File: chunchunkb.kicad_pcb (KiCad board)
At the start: 2 copper layers, 143.7 x 119.1 mm, 124 parts, among them J1 BATT, J2 OLED, SW1 SW_Push, SW10 SW_Push, SW11 SW_Push, SW12 SW_Push, SW13 SW_Push, SW14 SW_Push, SW15 SW_Push, SW16 SW_Push, SW17 SW_Push, SW18 SW_Push, SW19 SW_Push, SW2 SW_Push, SW20 SW_Push, SW21 SW_Push, SW22 SW_Push, SW23 SW_Push, SW24 SW_Push, SW25 SW_Push, SW26 SW_Push, SW27 SW_Push, SW28 SW_Push, SW29 SW_Push, SW3 SW_Push, SW30 SW_Push, SW31 EC11, SW32 SW_Push, SW33 SW_Push, SW34 SW_Push, SW35 SW_Push, SW36 SW_Push, SW4 SW_Push, SW5 SW_Push, SW6 SW_Push, SW7 SW_Push, SW8 SW_Push, SW9 SW_Push

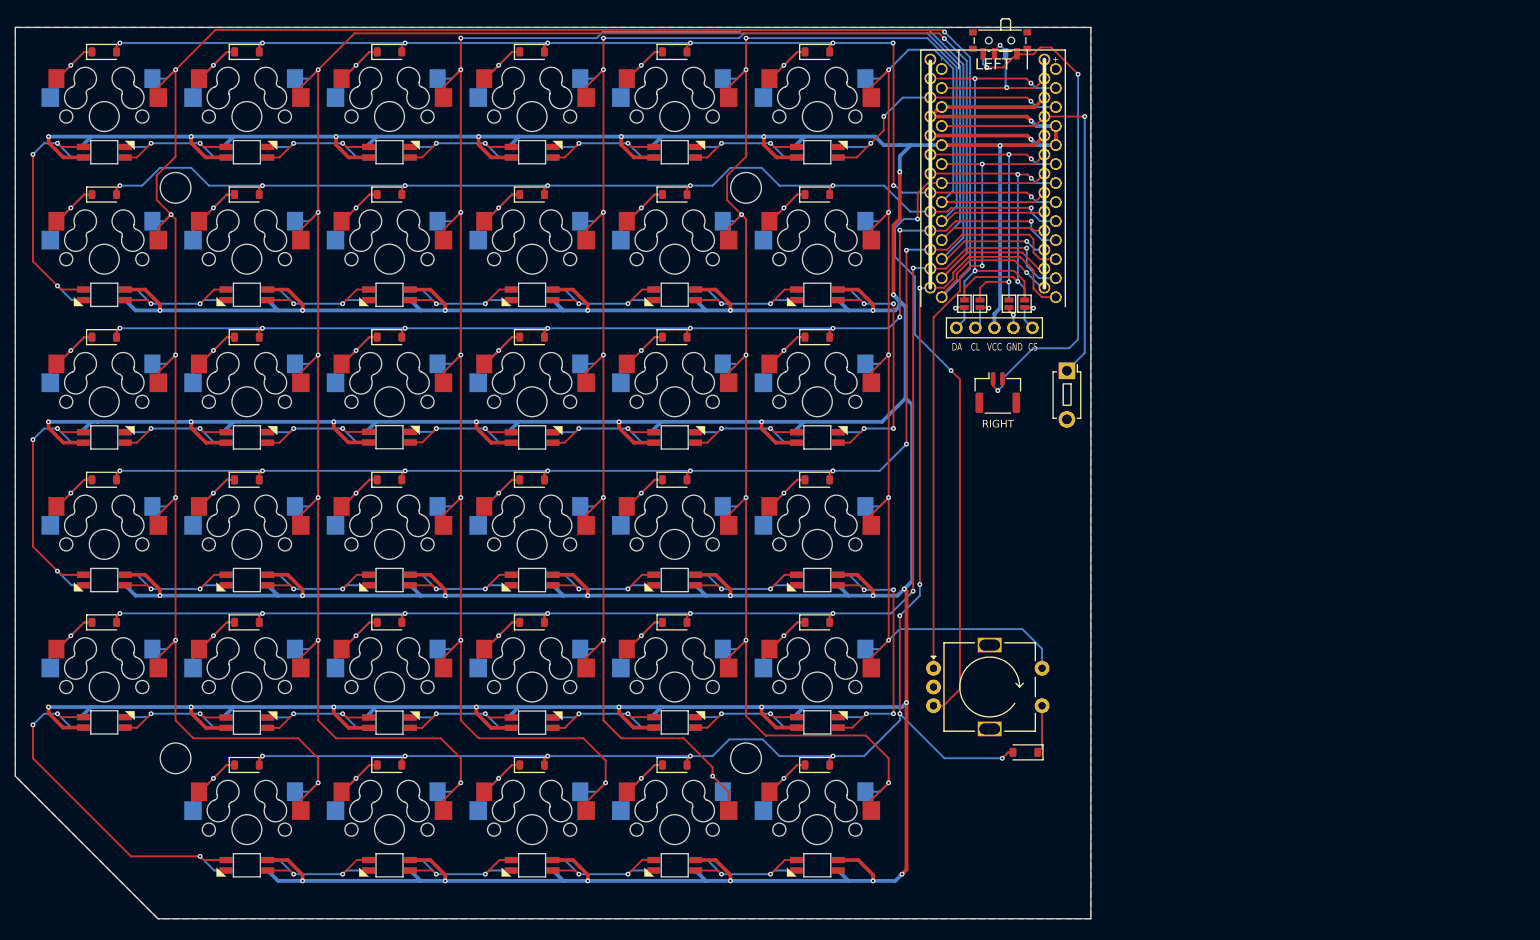
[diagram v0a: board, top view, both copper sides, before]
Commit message: feat: change space btn pos
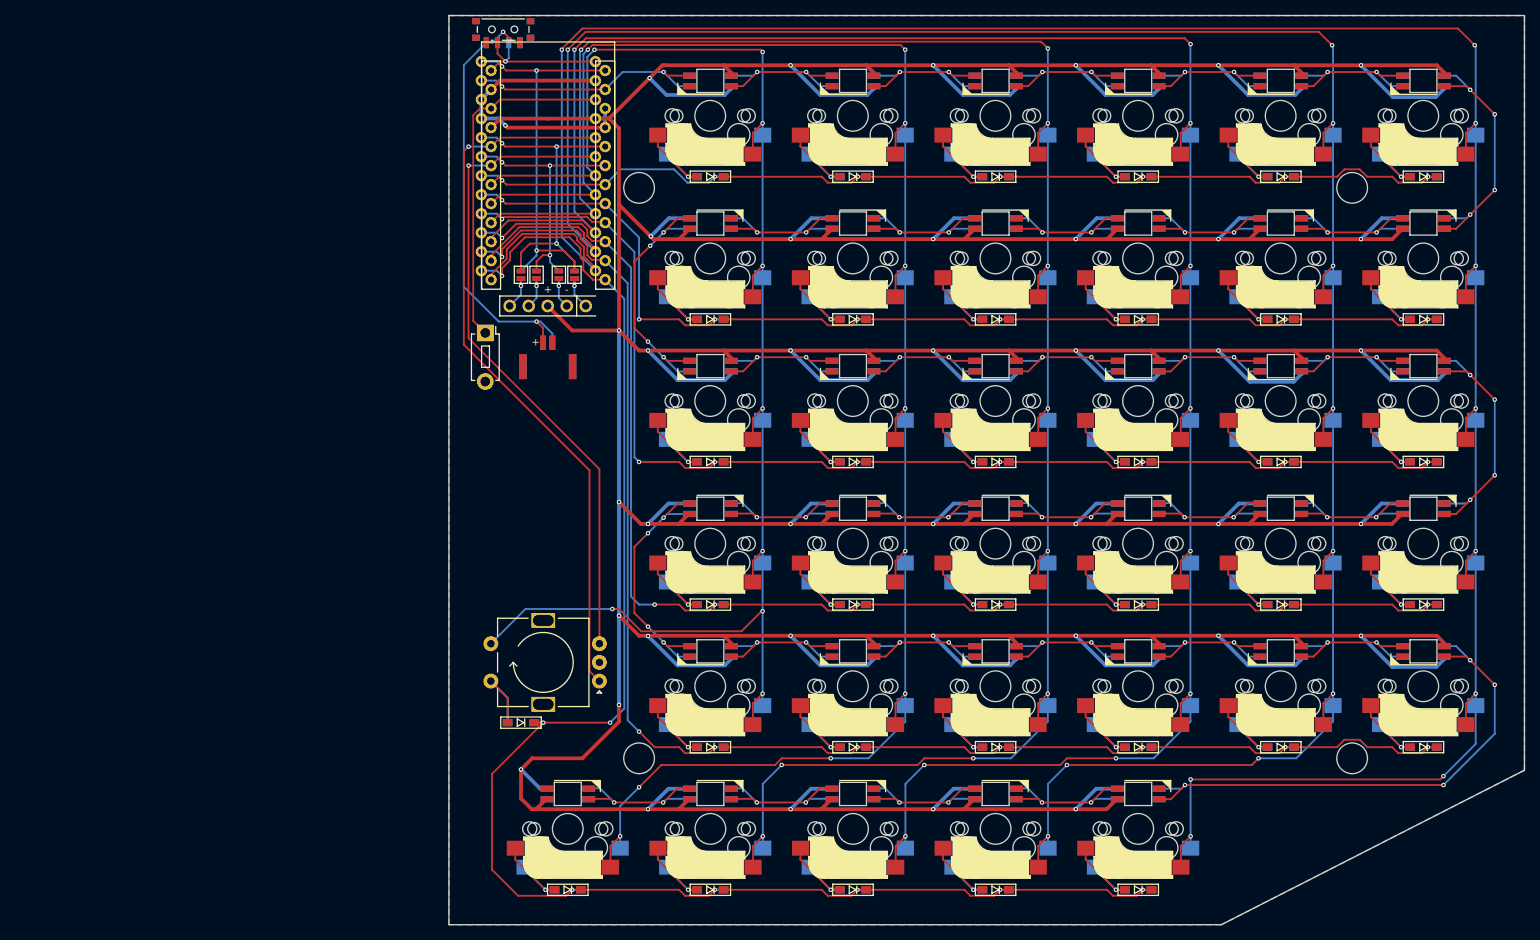
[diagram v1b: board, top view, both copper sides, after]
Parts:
- D1, D10, D11, D12, D13, D14, D15, D16, D17, D18, D19, D2, D20, D21, D22, D23, D24, D25, D26, D27, D28, D29, D3, D30, D31, D32, D33, D34, D35, D36, D4, D5, D6, D7, D8, D9: footprint chunchunkb:D_SOD-123 -> chunchunkb:crkbd-diode
- U1: footprint chunchunkb:ProMicro_DUAL -> chunchunkb:ProMicro DUAL
- moved D30 177.0 mm to (209.5, 117.6), turned to 180 degrees
- moved D24 177.0 mm to (209.5, 98.5), turned to 180 degrees
- moved D18 177.0 mm to (209.5, 79.5), turned to 180 degrees
- moved D12 177.0 mm to (209.5, 60.4), turned to 180 degrees
- moved D6 177.0 mm to (209.5, 41.4), turned to 180 degrees
- moved LED7 176.5 mm to (209.5, 47.6), turned to 180 degrees
- moved LED18 176.5 mm to (209.5, 66.7), turned to 0 degrees
- moved LED19 176.5 mm to (209.5, 85.7), turned to 180 degrees
- moved LED6 176.5 mm to (209.5, 28.6), turned to 0 degrees
- moved LED30 176.5 mm to (209.5, 104.8), turned to 0 degrees
- moved SW12 176.2 mm to (209.5, 52.3), turned to 180 degrees
- moved SW18 176.2 mm to (209.5, 71.3), turned to 180 degrees
- moved SW24 176.2 mm to (209.5, 90.4), turned to 180 degrees
- moved SW30 176.2 mm to (209.5, 109.4), turned to 180 degrees
- moved SW6 176.2 mm to (209.5, 33.2), turned to 180 degrees
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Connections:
- D1 pad 1: Net-(D1-K) -> ROW 0
- D1 pad 2: ROW 0 -> Net-(D1-A)
- D10 pad 1: Net-(D10-K) -> ROW 1
- D10 pad 2: ROW 1 -> Net-(D10-A)
- D11 pad 1: Net-(D11-K) -> ROW 1
- D11 pad 2: ROW 1 -> Net-(D11-A)
- D12 pad 1: Net-(D12-K) -> ROW 1
- D12 pad 2: ROW 1 -> Net-(D12-A)
- D13 pad 1: Net-(D13-K) -> ROW 2
- D13 pad 2: ROW 2 -> Net-(D13-A)
- D14 pad 1: Net-(D14-K) -> ROW 2
- D14 pad 2: ROW 2 -> Net-(D14-A)
- D15 pad 1: Net-(D15-K) -> ROW 2
- D15 pad 2: ROW 2 -> Net-(D15-A)
- D16 pad 1: Net-(D16-K) -> ROW 2
- D16 pad 2: ROW 2 -> Net-(D16-A)
- D17 pad 1: Net-(D17-K) -> ROW 2
- D17 pad 2: ROW 2 -> Net-(D17-A)
- D18 pad 1: Net-(D18-K) -> ROW 2
- D18 pad 2: ROW 2 -> Net-(D18-A)
- D19 pad 1: Net-(D19-K) -> ROW 3
- D19 pad 2: ROW 3 -> Net-(D19-A)
- D2 pad 1: Net-(D2-K) -> ROW 0
- D2 pad 2: ROW 0 -> Net-(D2-A)
- D20 pad 1: Net-(D20-K) -> ROW 3
- D20 pad 2: ROW 3 -> Net-(D20-A)
- D21 pad 1: Net-(D21-K) -> ROW 3
- D21 pad 2: ROW 3 -> Net-(D21-A)
- D22 pad 1: Net-(D22-K) -> ROW 3
- D22 pad 2: ROW 3 -> Net-(D22-A)
- D23 pad 1: Net-(D23-K) -> ROW 3
- D23 pad 2: ROW 3 -> Net-(D23-A)
- D24 pad 1: Net-(D24-K) -> ROW 3
- D24 pad 2: ROW 3 -> Net-(D24-A)
- D25 pad 1: Net-(D25-K) -> ROW 4
- D25 pad 2: ROW 4 -> Net-(D25-A)
- D26 pad 1: Net-(D26-K) -> ROW 4
- D26 pad 2: ROW 4 -> Net-(D26-A)
- D27 pad 1: Net-(D27-K) -> ROW 4
- D27 pad 2: ROW 4 -> Net-(D27-A)
- D28 pad 1: Net-(D28-K) -> ROW 4
- D28 pad 2: ROW 4 -> Net-(D28-A)
- D29 pad 1: Net-(D29-K) -> ROW 4
- D29 pad 2: ROW 4 -> Net-(D29-A)
- D3 pad 1: Net-(D3-K) -> ROW 0
- D3 pad 2: ROW 0 -> Net-(D3-A)
- D30 pad 1: Net-(D30-K) -> ROW 4
- D30 pad 2: ROW 4 -> Net-(D30-A)
- D31 pad 1: SW31A -> ROW 5
- D31 pad 2: ROW 5 -> SW31B
- D32 pad 1: Net-(D32-K) -> ROW 5
- D32 pad 2: ROW 5 -> Net-(D32-A)
- D33 pad 1: Net-(D33-K) -> ROW 5
- D33 pad 2: ROW 5 -> Net-(D33-A)
- D34 pad 1: Net-(D34-K) -> ROW 5
- D34 pad 2: ROW 5 -> Net-(D34-A)
- D35 pad 1: Net-(D35-K) -> ROW 5
- D35 pad 2: ROW 5 -> Net-(D35-A)
- D36 pad 1: Net-(D36-K) -> ROW 5
- D36 pad 2: ROW 5 -> Net-(D36-A)
- D4 pad 1: Net-(D4-K) -> ROW 0
- D4 pad 2: ROW 0 -> Net-(D4-A)
- D5 pad 1: Net-(D5-K) -> ROW 0
- D5 pad 2: ROW 0 -> Net-(D5-A)
- D6 pad 1: Net-(D6-K) -> ROW 0
- D6 pad 2: ROW 0 -> Net-(D6-A)
- D7 pad 1: Net-(D7-K) -> ROW 1
- D7 pad 2: ROW 1 -> Net-(D7-A)
- D8 pad 1: Net-(D8-K) -> ROW 1
- D8 pad 2: ROW 1 -> Net-(D8-A)
- D9 pad 1: Net-(D9-K) -> ROW 1
- D9 pad 2: ROW 1 -> Net-(D9-A)
- JP3 pad 2: MOSI/SDA -> SCK/SCL
- JP4 pad 2: SCK/SCL -> MOSI/SDA
- JP7 pad 2: MOSI/SDA -> SCK/SCL
- JP8 pad 2: SCK/SCL -> MOSI/SDA
- SW1 pad 1: Net-(D1-K) -> COL 0
- SW1 pad 2: COL 0 -> Net-(D1-A)
- SW10 pad 1: Net-(D10-K) -> COL 3
- SW10 pad 2: COL 3 -> Net-(D10-A)
- SW11 pad 1: Net-(D11-K) -> COL 4
- SW11 pad 2: COL 4 -> Net-(D11-A)
- SW12 pad 1: Net-(D12-K) -> COL 5
- SW12 pad 2: COL 5 -> Net-(D12-A)
- SW13 pad 1: Net-(D13-K) -> COL 0
- SW13 pad 2: COL 0 -> Net-(D13-A)
- SW14 pad 1: Net-(D14-K) -> COL 1
- SW14 pad 2: COL 1 -> Net-(D14-A)
- SW15 pad 1: Net-(D15-K) -> COL 2
- SW15 pad 2: COL 2 -> Net-(D15-A)
- SW16 pad 1: Net-(D16-K) -> COL 3
- SW16 pad 2: COL 3 -> Net-(D16-A)
- SW17 pad 1: Net-(D17-K) -> COL 4
- SW17 pad 2: COL 4 -> Net-(D17-A)
- SW18 pad 1: Net-(D18-K) -> COL 5
- SW18 pad 2: COL 5 -> Net-(D18-A)
- SW19 pad 1: Net-(D19-K) -> COL 0
- SW19 pad 2: COL 0 -> Net-(D19-A)
- SW2 pad 1: Net-(D2-K) -> COL 1
- SW2 pad 2: COL 1 -> Net-(D2-A)
- SW20 pad 1: Net-(D20-K) -> COL 1
- SW20 pad 2: COL 1 -> Net-(D20-A)
- SW21 pad 1: Net-(D21-K) -> COL 2
- SW21 pad 2: COL 2 -> Net-(D21-A)
- SW22 pad 1: Net-(D22-K) -> COL 3
- SW22 pad 2: COL 3 -> Net-(D22-A)
- SW23 pad 1: Net-(D23-K) -> COL 4
- SW23 pad 2: COL 4 -> Net-(D23-A)
- SW24 pad 1: Net-(D24-K) -> COL 5
- SW24 pad 2: COL 5 -> Net-(D24-A)
- SW25 pad 1: Net-(D25-K) -> COL 0
- SW25 pad 2: COL 0 -> Net-(D25-A)
- SW26 pad 1: Net-(D26-K) -> COL 1
- SW26 pad 2: COL 1 -> Net-(D26-A)
- SW27 pad 1: Net-(D27-K) -> COL 2
- SW27 pad 2: COL 2 -> Net-(D27-A)
- SW28 pad 1: Net-(D28-K) -> COL 3
- SW28 pad 2: COL 3 -> Net-(D28-A)
- SW29 pad 1: Net-(D29-K) -> COL 4
- SW29 pad 2: COL 4 -> Net-(D29-A)
- SW3 pad 1: Net-(D3-K) -> COL 2
- SW3 pad 2: COL 2 -> Net-(D3-A)
- SW30 pad 1: Net-(D30-K) -> COL 5
- SW30 pad 2: COL 5 -> Net-(D30-A)
- SW31 pad S1: SW31A -> COL 0
- SW31 pad S2: COL 0 -> SW31B
- SW32 pad 1: Net-(D32-K) -> COL 1
- SW32 pad 2: COL 1 -> Net-(D32-A)
- SW33 pad 1: Net-(D33-K) -> COL 2
- SW33 pad 2: COL 2 -> Net-(D33-A)
- SW34 pad 1: Net-(D34-K) -> COL 3
- SW34 pad 2: COL 3 -> Net-(D34-A)
- SW35 pad 1: Net-(D35-K) -> COL 4
- SW35 pad 2: COL 4 -> Net-(D35-A)
- SW36 pad 1: Net-(D36-K) -> COL 5
- SW36 pad 2: COL 5 -> Net-(D36-A)
- SW4 pad 1: Net-(D4-K) -> COL 3
- SW4 pad 2: COL 3 -> Net-(D4-A)
- SW5 pad 1: Net-(D5-K) -> COL 4
- SW5 pad 2: COL 4 -> Net-(D5-A)
- SW6 pad 1: Net-(D6-K) -> COL 5
- SW6 pad 2: COL 5 -> Net-(D6-A)
- SW7 pad 1: Net-(D7-K) -> COL 0
- SW7 pad 2: COL 0 -> Net-(D7-A)
- SW8 pad 1: Net-(D8-K) -> COL 1
- SW8 pad 2: COL 1 -> Net-(D8-A)
- SW9 pad 1: Net-(D9-K) -> COL 2
- SW9 pad 2: COL 2 -> Net-(D9-A)
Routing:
- net VCC: track 1065.2 -> 1168.6 mm, vias 41 -> 39
- net COL 5: track 323.1 -> 346.9 mm, vias 8 -> 10
- net COL 4: track 297.5 -> 319.0 mm, vias 7 -> 10
- net COL 2: track 247.5 -> 268.5 mm, vias 7 -> 10
- net ROW 0: track 161.4 -> 141.2 mm, vias 9 -> 12
- net COL 0: track 185.8 -> 205.9 mm, vias 5 -> 9
- net Net-(LED30-DOUT): track 51.8 -> 71.2 mm, vias 3 -> 4
- net Net-(D17-K): track 17.7 -> 0.00 mm, vias 1 -> 0
- net Net-(D15-K): track 17.7 -> 0.00 mm, vias 1 -> 0
- net GND: track 56.0 -> 38.5 mm, vias 2 -> 1
- net COL 3: track 277.5 -> 293.6 mm, vias 8 -> 10
- net ROW 4: track 190.1 -> 205.7 mm, vias 9 -> 8
- net Net-(D30-K): track 15.2 -> 0.00 mm, vias 1 -> 0
- net Net-(D36-K): track 15.2 -> 0.00 mm, vias 1 -> 0
- net Net-(D29-K): track 15.2 -> 0.00 mm, vias 1 -> 0
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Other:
- board size 143.7 x 119.1 mm -> 143.7 x 121.4 mm
- rule pad_to_mask_clearance: 0.2 -> 0

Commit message: rev 2
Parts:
- added LED36: YS-SK6812MINI-E, chunchunkb:YS-SK6812MINI-E, F.Cu at (161.9, 109.5)
- SW31: footprint chunchunkb:EC11_Switch -> chunchunkb:EC11_MX_Hybrid
- U1: footprint chunchunkb:ProMicro DUAL -> chunchunkb:ProMicro_DUAL
- moved SW_POWER1 176.9 mm to (256.0, 73.2), turned to 0 degrees
- moved LED7 162.0 mm to (47.6, 52.4), turned to 0 degrees
- moved LED19 162.0 mm to (47.6, 90.5), turned to 0 degrees
- moved LED18 162.0 mm to (47.6, 71.4), turned to 180 degrees
- moved LED30 162.0 mm to (47.6, 109.5), turned to 180 degrees
- moved LED6 162.0 mm to (47.6, 33.3), turned to 180 degrees
- moved SW12 162.0 mm to (47.6, 57.1)
- moved SW18 162.0 mm to (47.6, 76.2)
- moved SW24 162.0 mm to (47.6, 95.2)
- moved SW30 162.0 mm to (47.6, 114.3)
- moved SW6 162.0 mm to (47.6, 38.1)
- moved D12 155.5 mm to (54.2, 65.8)
- moved D18 155.5 mm to (54.2, 84.8)
- moved D24 155.5 mm to (54.2, 103.9)
- moved D30 155.5 mm to (54.2, 122.9)
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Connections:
- LED35 pad 2: unconnected-(LED35-DOUT-Pad2) -> Net-(LED35-DOUT)
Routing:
- net COL 5: track 346.9 -> 150.2 mm, vias 10 -> 7
- net COL 4: track 319.0 -> 147.6 mm, vias 10 -> 7
- net COL 3: track 293.6 -> 145.4 mm, vias 10 -> 7
- net COL 2: track 268.5 -> 145.4 mm, vias 10 -> 7
- net VCC: track 1168.6 -> 1062.2 mm, vias 39 -> 38
- net COL 1: track 243.8 -> 145.4 mm, vias 10 -> 7
- net ENC A: track 96.6 -> 9.65 mm
- net ROW 4: track 205.7 -> 119.0 mm, vias 8 -> 7
- net ENC B: track 88.6 -> 9.65 mm
- net ROW 5: track 217.3 -> 139.4 mm, vias 8 -> 7
- net ROW 3: track 187.1 -> 117.3 mm, vias 8 -> 7
- net Net-(J1-Pin_1): track 58.3 -> 0.00 mm, vias 2 -> 0
- net ROW 2: track 168.7 -> 117.3 mm, vias 8 -> 7
- net COL 0: track 205.9 -> 159.3 mm, vias 9 -> 8
- net RESET: track 46.9 -> 9.65 mm, vias 0 -> 1
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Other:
- board size 143.7 x 121.4 mm -> 162.8 x 134.8 mm

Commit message: rem large
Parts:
- moved SW_POWER1 94.8 mm to (164.3, 49.1), turned to 180 degrees
- moved SW_RST1 54.5 mm to (171.7, 90.5), turned to -90 degrees
- moved J1 53.9 mm to (164.3, 93.0)
- moved JP1 2.02 mm to (167.9, 83.1)
- moved JP4 2.02 mm to (160.5, 83.1)
- moved JP5 2.02 mm to (160.5, 83.1)
- moved JP8 2.02 mm to (167.9, 83.1)
- moved J2 2.02 mm to (164.2, 70.0)
- moved JP2 2.02 mm to (166.1, 83.1)
- moved JP3 2.02 mm to (162.3, 83.1)
- moved JP6 2.02 mm to (162.3, 83.1)
- moved JP7 2.02 mm to (166.1, 83.1)
- moved U1 2.02 mm to (164.2, 67.2)
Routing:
- net COL 5: track 150.2 -> 284.3 mm, vias 7 -> 10
- net COL 4: track 147.6 -> 265.8 mm, vias 7 -> 10
- net VCC: track 1062.2 -> 1172.2 mm, vias 38 -> 44
- net COL 3: track 145.4 -> 246.0 mm, vias 7 -> 10
- net ENC A: track 9.65 -> 91.2 mm, vias 1 -> 4
- net COL 2: track 145.4 -> 224.2 mm, vias 7 -> 10
- net ENC B: track 9.65 -> 82.2 mm, vias 1 -> 4
- net Net-(J1-Pin_1): track 0.00 -> 66.3 mm, vias 0 -> 3
- net COL 1: track 145.4 -> 204.1 mm, vias 7 -> 10
- net ROW 4: track 119.0 -> 170.3 mm, vias 7 -> 8
- net ROW 3: track 117.3 -> 154.1 mm, vias 7 -> 8
- net ROW 5: track 139.4 -> 176.0 mm, vias 7 -> 8
- net RESET: track 9.65 -> 46.0 mm
- net Net-(LED35-DOUT): track 0.00 -> 34.2 mm, vias 0 -> 2
- net COL 0: track 159.3 -> 193.1 mm, vias 8 -> 11
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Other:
- board size 162.8 x 134.8 mm -> 139.6 x 119.1 mm
